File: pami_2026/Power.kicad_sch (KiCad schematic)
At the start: 34 parts, among them J1 Conn_01x02_Pin, Q1 PMOS, U2 AP63205WU, U3 DRV8871DDA, U5 AP63203WU, U6 DRV8871DDA

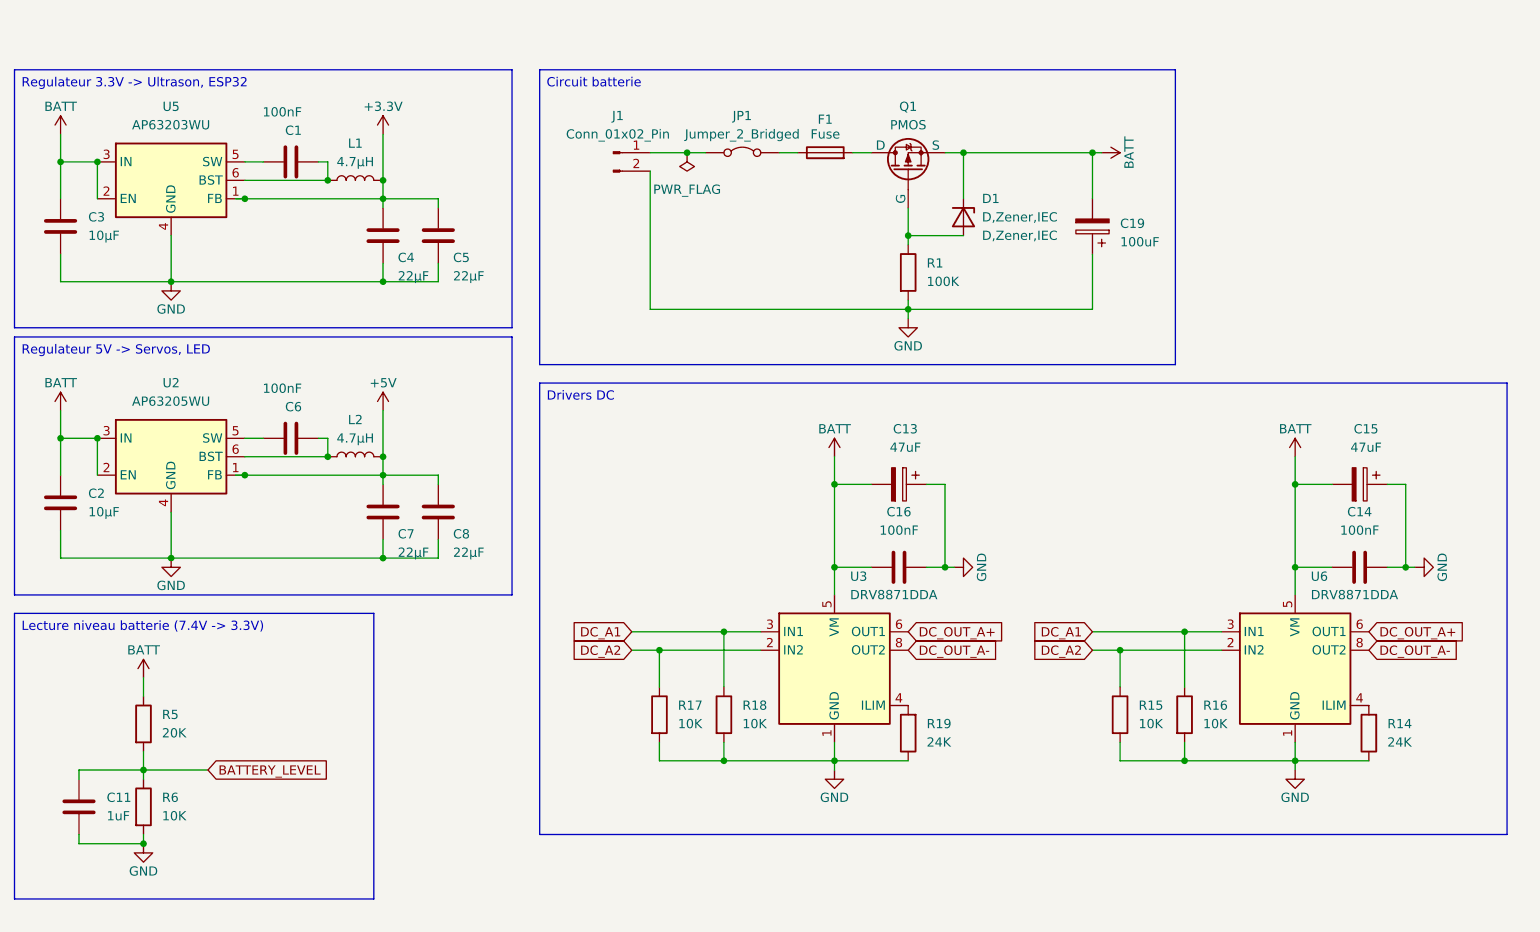
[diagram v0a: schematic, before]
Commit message: Fix: ERC is Happy - proper footprints - Feat: add multiplexer for external power
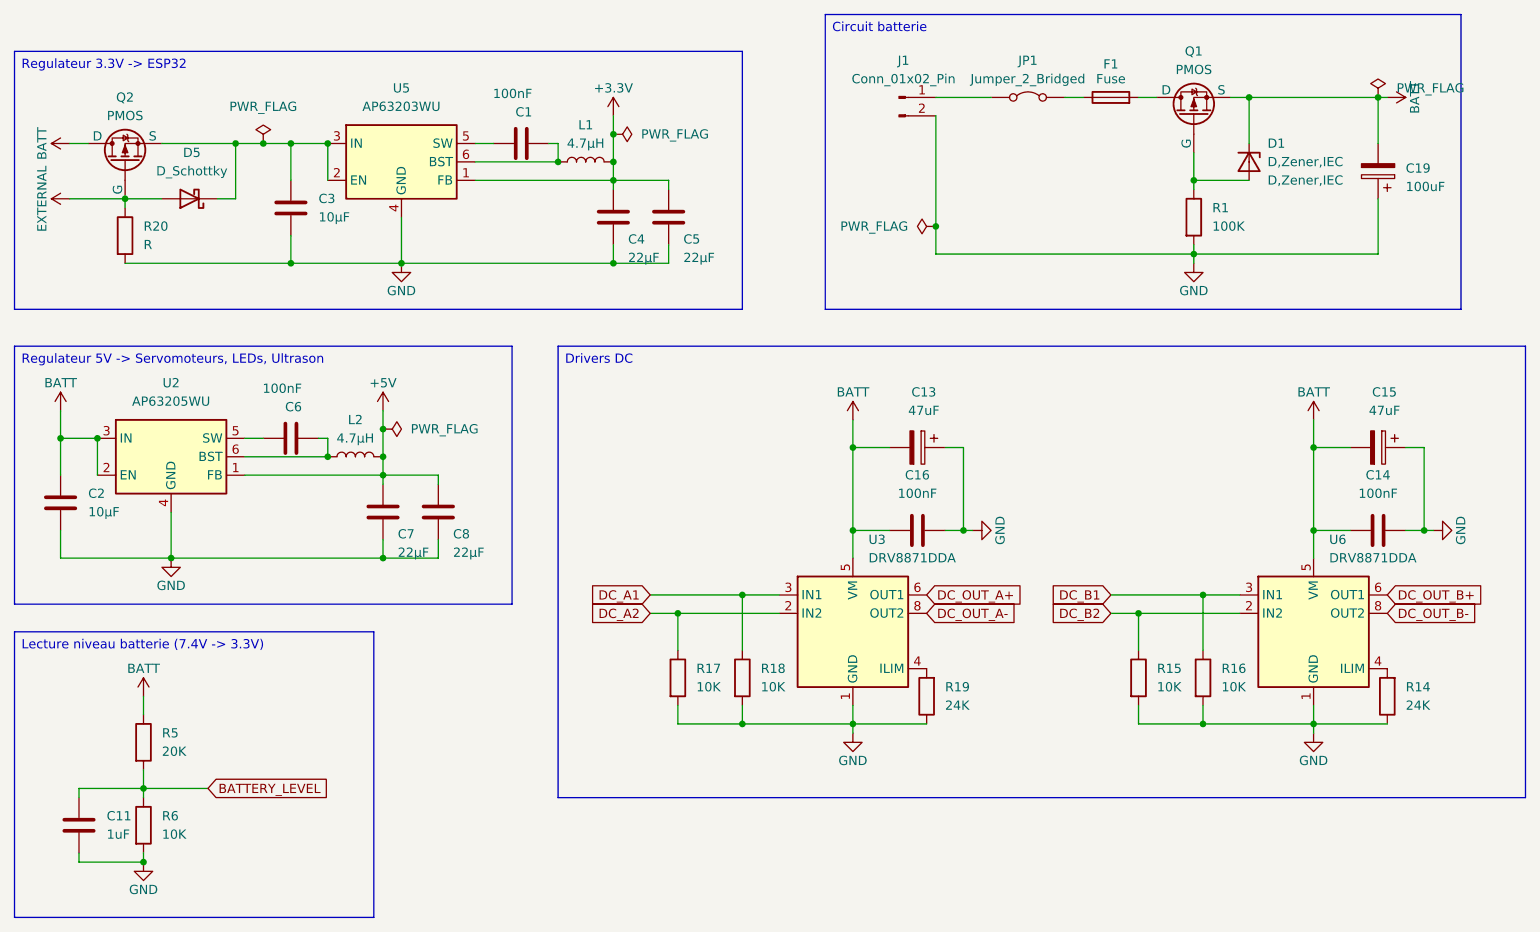
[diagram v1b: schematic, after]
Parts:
- added D5: D_Schottky, symbol Device:D_Schottky
- added Q2: PMOS, symbol Simulation_SPICE:PMOS
- added R20: R, symbol Device:R
- C13, C15: footprint (none) -> PCM_SparkFun-Capacitor:Panasonic_F
- C19: footprint Capacitor_SMD:C_0603_1608Metric -> PCM_SparkFun-Capacitor:CAP_EEETC1C101V
- R14, R17, R18: footprint PCM_SparkFun-Resistor:R_0603_1608Metric -> Resistor_SMD:R_0201_0603Metric
- R15, R16, R19: footprint PCM_SparkFun-Resistor:R_0603_1608Metric -> Resistor_SMD:R_0603_1608Metric
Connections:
- net BATT: now also Q2.1 (D); no longer C3.1, U5.2 (EN), U5.3 (IN)
- net DC_A1: no longer R16.1, U6.3 (IN1)
- net DC_A2: no longer R15.1, U6.2 (IN2)
- net DC_OUT_A+: no longer U6.6 (OUT1)
- net DC_OUT_A-: no longer U6.8 (OUT2)
- net GND: now also R20.2
- new net: C3.1, D5.1 (K), Q2.3 (S), U5.2 (EN), U5.3 (IN)
- new net DC_B1: R16.1, U6.3 (IN1)
- new net DC_B2: R15.1, U6.2 (IN2)
- new net DC_OUT_B+: U6.6 (OUT1)
- new net DC_OUT_B-: U6.8 (OUT2)
- new net EXTERNAL: D5.2 (A), Q2.2 (G), R20.1
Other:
- moved on the sheet: C1, C11, C13, C14, C15, C16, C19, C3, C4, C5, D1, F1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

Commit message: fix footprints
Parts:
- D5: footprint (none) -> Diode_SMD:D_SOD-123
- Q2: footprint (none) -> Package_TO_SOT_SMD:SOT-223
- R20: value R -> 10K; footprint (none) -> Resistor_SMD:R_0201_0603Metric
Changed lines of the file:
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@@
 			)
 		)
-		(property "Value" "R"
+		(property "Value" "10K"
 			(at 34.29 46.9899 0)
 			(effects
@@
 			)
 		)
-		(property "Footprint" ""
+		(property "Footprint" "Resistor_SMD:R_0201_0603Metric"
 			(at 29.972 45.72 90)
 			(effects
@@
 			)
 		)
-		(property "Footprint" ""
+		(property "Footprint" "Diode_SMD:D_SOD-123"
 			(at 40.64 40.64 0)
 			(effects
@@
 			)
 		)
-		(property "Footprint" ""
+		(property "Footprint" "Package_TO_SOT_SMD:SOT-223"
 			(at 29.21 30.48 0)
 			(effects

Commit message: FEAT : Routing
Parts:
- removed JP1: Jumper_2_Bridged, Jumper:SolderJumper-2_P1.3mm_Bridged_RoundedPad1.0x1.5mm, symbol Jumper:Jumper_2_Bridged
- added J9: Conn_01x02_Pin, Connector_PinHeader_2.54mm:PinHeader_1x02_P2.54mm_Vertical, symbol Connector:Conn_01x02_Pin
- C19: footprint PCM_SparkFun-Capacitor:CAP_EEETC1C101V -> lib:CAP_EEETC1C101V
- J1: footprint Connector_PinHeader_2.54mm:PinHeader_1x01_P2.54mm_Vertical -> Connector_PinHeader_2.54mm:PinHeader_1x02_P2.54mm_Vertical
- R14, R17, R18, R20: footprint Resistor_SMD:R_0201_0603Metric -> Resistor_SMD:R_0603_1608Metric
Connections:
- net at F1.1: now also J9.1 (Pin_1)
- net at J1.1 (Pin_1): now also J9.2 (Pin_2)
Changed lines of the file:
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@@
 	(wire
 		(pts
+			(xy 157.48 26.67) (xy 163.83 26.67)
+		)
+		(stroke
+			(width 0)
+			(type default)
+		)
+	)
+	(wire
+		(pts
 			(xy 59.69 33.02) (xy 59.69 38.1)
 		)
@@
 	(wire
 		(pts
-			(xy 161.29 26.67) (xy 163.83 26.67)
-		)
-		(stroke
-			(width 0)
-			(type default)
-		)
-	)
-	(wire
-		(pts
 			(xy 107.95 97.79) (xy 107.95 102.87)
 		)
@@
 	(wire
 		(pts
-			(xy 143.51 26.67) (xy 151.13 26.67)
+			(xy 143.51 26.67) (xy 154.94 26.67)
 		)
 		(stroke
@@
 			)
 		)
-		(property "Footprint" "Resistor_SMD:R_0201_0603Metric"
+		(property "Footprint" "Resistor_SMD:R_0603_1608Metric"
 			(at 29.972 45.72 90)
 			(effects
@@
 			)
 		)
-		(property "Footprint" "PCM_SparkFun-Capacitor:CAP_EEETC1C101V"
+		(property "Footprint" "lib:CAP_EEETC1C101V"
 			(at 203.5048 33.02 0)
 			(effects
@@
 			)
 		)
-		(property "Footprint" "Resistor_SMD:R_0201_0603Metric"
+		(property "Footprint" "Resistor_SMD:R_0603_1608Metric"
 			(at 106.172 106.68 90)
 			(effects
@@
 	)
 	(symbol
-		(lib_id "Jumper:Jumper_2_Bridged")
-		(at 156.21 26.67 0)
-		(unit 1)
-		(exclude_from_sim no)
-		(in_bom yes)
-		(on_board yes)
-		(dnp no)
-		(fields_autoplaced yes)
-		(property "Reference" "JP1"
-			(at 156.21 21.59 0)
-			(effects
-				(font
-					(size 1.27 1.27)
-				)
-			)
-		)
-		(property "Value" "Jumper_2_Bridged"
-			(at 156.21 24.13 0)
-			(effects
-				(font
-					(size 1.27 1.27)
-				)
-			)
-		)
-		(property "Footprint" "Jumper:SolderJumper-2_P1.3mm_Bridged_RoundedPad1.0x1.5mm"
-			(at 156.21 26.67 0)
-			(effects
-				(font
-					(size 1.27 1.27)
-				)
-				(hide yes)
-			)
-		)
-		(property "Datasheet" "~"
-			(at 156.21 26.67 0)
-			(effects
-				(font
-					(size 1.27 1.27)
-				)
-				(hide yes)
-			)
-		)
-		(property "Description" "Jumper, 2-pole, closed/bridged"
-			(at 156.21 26.67 0)
-			(effects
-				(font
-					(size 1.27 1.27)
-				)
-				(hide yes)
-			)
-		)
-		(pin "1"
-		)
-		(pin "2"
-		)
-		(instances
-			(project ""
-				(path "/2e16a05b-e8ca-4fff-9c3e-5c880745daa6/ed527990-c321-4ebf-9ae6-9a3c892317c7"
-					(reference "JP1")
-					(unit 1)
-				)
-			)
-		)
-	)
-	(symbol
 		(lib_id "PCM_SparkFun-PowerSymbol:VCC")
 		(at 205.74 26.67 270)
@@
 			)
 		)
-		(property "Footprint" "Connector_PinHeader_2.54mm:PinHeader_1x01_P2.54mm_Vertical"
+		(property "Footprint" "Connector_PinHeader_2.54mm:PinHeader_1x02_P2.54mm_Vertical"
 			(at 138.43 26.67 0)
 			(effects
@@
 	)
 	(symbol
+		(lib_id "Connector:Conn_01x02_Pin")
+		(at 157.48 21.59 270)
+		(unit 1)
+		(exclude_from_sim no)
+		(in_bom yes)
+		(on_board yes)
+		(dnp no)
+		(fields_autoplaced yes)
+		(property "Reference" "J9"
+			(at 158.75 20.9549 90)
+			(effects
+				(font
+					(size 1.27 1.27)
+				)
+				(justify left)
+			)
+		)
+		(property "Value" "Conn_01x02_Pin"
+			(at 158.75 23.4949 90)
+			(effects
+				(font
+					(size 1.27 1.27)
+				)
+				(justify left)
+			)
+		)
+		(property "Footprint" "Connector_PinHeader_2.54mm:PinHeader_1x02_P2.54mm_Vertical"
+			(at 157.48 21.59 0)
+			(effects
+				(font
+					(size 1.27 1.27)
+				)
+				(hide yes)
+			)
+		)
+		(property "Datasheet" "~"
+			(at 157.48 21.59 0)
+			(effects
+				(font
+					(size 1.27 1.27)
+				)
+				(hide yes)
+			)
+		)
+		(property "Description" "Generic connector, single row, 01x02, script generated"
+			(at 157.48 21.59 0)
+			(effects
+				(font
+					(size 1.27 1.27)
+				)
+				(hide yes)
+			)
+		)
+		(pin "1"
+		)
+		(pin "2"
+		)
+		(instances
+			(project "pami_2026"
+				(path "/2e16a05b-e8ca-4fff-9c3e-5c880745daa6/ed527990-c321-4ebf-9ae6-9a3c892317c7"
+					(reference "J9")
+					(unit 1)
+				)
+			)
+		)
+	)
+	(symbol
 		(lib_id "Device:R")
 		(at 171.45 106.68 0)
@@
 			)
 		)
-		(property "Footprint" "Resistor_SMD:R_0201_0603Metric"
+		(property "Footprint" "Resistor_SMD:R_0603_1608Metric"
 			(at 115.062 106.68 90)
 			(effects
@@
 			)
 		)
-		(property "Footprint" "Resistor_SMD:R_0201_0603Metric"
+		(property "Footprint" "Resistor_SMD:R_0603_1608Metric"
 			(at 207.518 109.22 90)
 			(effects

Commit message: Feat: mounting holes, indications, fix capa polarity
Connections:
- net BATT: now also C13.1, C15.1, C19.1; no longer C13.2, C15.2, C19.2
- net GND: now also C13.2, C15.2, C19.2; no longer C13.1, C15.1, C19.1
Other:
- moved on the sheet: C13, C15, C19
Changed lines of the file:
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@@
 	(symbol
 		(lib_id "Device:C_Polarized")
-		(at 204.47 36.83 180)
-		(unit 1)
-		(exclude_from_sim no)
-		(in_bom yes)
-		(on_board yes)
-		(dnp no)
-		(fields_autoplaced yes)
+		(at 204.47 36.83 0)
+		(mirror y)
+		(unit 1)
+		(exclude_from_sim no)
+		(in_bom yes)
+		(on_board yes)
+		(dnp no)
 		(property "Reference" "C19"
-			(at 208.28 36.4489 0)
+			(at 208.28 37.2111 0)
 			(effects
 				(font
@@
 		)
 		(property "Value" "100uF"
-			(at 208.28 38.9889 0)
+			(at 208.28 34.6711 0)
 			(effects
 				(font
@@
 		)
 		(property "Footprint" "lib:CAP_EEETC1C101V"
-			(at 203.5048 33.02 0)
+			(at 203.5048 40.64 0)
 			(effects
 				(font
@@
 	(symbol
 		(lib_id "Device:C_Polarized")
-		(at 140.97 74.93 270)
-		(unit 1)
-		(exclude_from_sim no)
-		(in_bom yes)
-		(on_board yes)
-		(dnp no)
-		(fields_autoplaced yes)
+		(at 140.97 74.93 90)
+		(mirror x)
+		(unit 1)
+		(exclude_from_sim no)
+		(in_bom yes)
+		(on_board yes)
+		(dnp no)
 		(property "Reference" "C13"
-			(at 141.859 67.31 90)
+			(at 140.081 67.31 90)
 			(effects
 				(font
@@
 		)
 		(property "Value" "47uF"
-			(at 141.859 69.85 90)
+			(at 140.081 69.85 90)
 			(effects
 				(font
@@
 		)
 		(property "Footprint" "PCM_SparkFun-Capacitor:Panasonic_F"
-			(at 137.16 75.8952 0)
+			(at 144.78 75.8952 0)
 			(effects
 				(font
@@
 	(symbol
 		(lib_id "Device:C_Polarized")
-		(at 204.47 74.93 270)
-		(unit 1)
-		(exclude_from_sim no)
-		(in_bom yes)
-		(on_board yes)
-		(dnp no)
-		(fields_autoplaced yes)
+		(at 204.47 74.93 90)
+		(mirror x)
+		(unit 1)
+		(exclude_from_sim no)
+		(in_bom yes)
+		(on_board yes)
+		(dnp no)
 		(property "Reference" "C15"
-			(at 205.359 67.31 90)
+			(at 203.581 67.31 90)
 			(effects
 				(font
@@
 		)
 		(property "Value" "47uF"
-			(at 205.359 69.85 90)
+			(at 203.581 69.85 90)
 			(effects
 				(font
@@
 		)
 		(property "Footprint" "PCM_SparkFun-Capacitor:Panasonic_F"
-			(at 200.66 75.8952 0)
+			(at 208.28 75.8952 0)
 			(show_name yes)
 			(effects

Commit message: Feat: BOM LCSC + big plan de masse
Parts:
- C1, C14, C16, C6: LCSC (none) -> C1591
- C11: LCSC (none) -> C15849
- C13, C15: LCSC (none) -> C128464
- C19: LCSC (none) -> C2163886
- C2, C3: LCSC (none) -> C15850
- C4, C5, C7, C8: LCSC (none) -> C602037
- D1: LCSC (none) -> C41408110
- D5: LCSC (none) -> C908229
- F1: LCSC (none) -> C48783168
- J1, J9: LCSC (none) -> C32713268
- L1, L2: LCSC (none) -> C6364810
- Q1, Q2: LCSC (none) -> C49066897
- R1: LCSC (none) -> C2906980
- R14, R19: LCSC (none) -> C2930081
- R15, R16, R17, R18, R20, R6: LCSC (none) -> C98220
- R5: LCSC (none) -> C105575
- U2: LCSC (none) -> C2071056
- U3, U6: LCSC (none) -> C701805
- U5: LCSC (none) -> C780769
